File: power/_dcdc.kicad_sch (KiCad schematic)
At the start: 13 parts, among them U5 TPS56A37RPAR

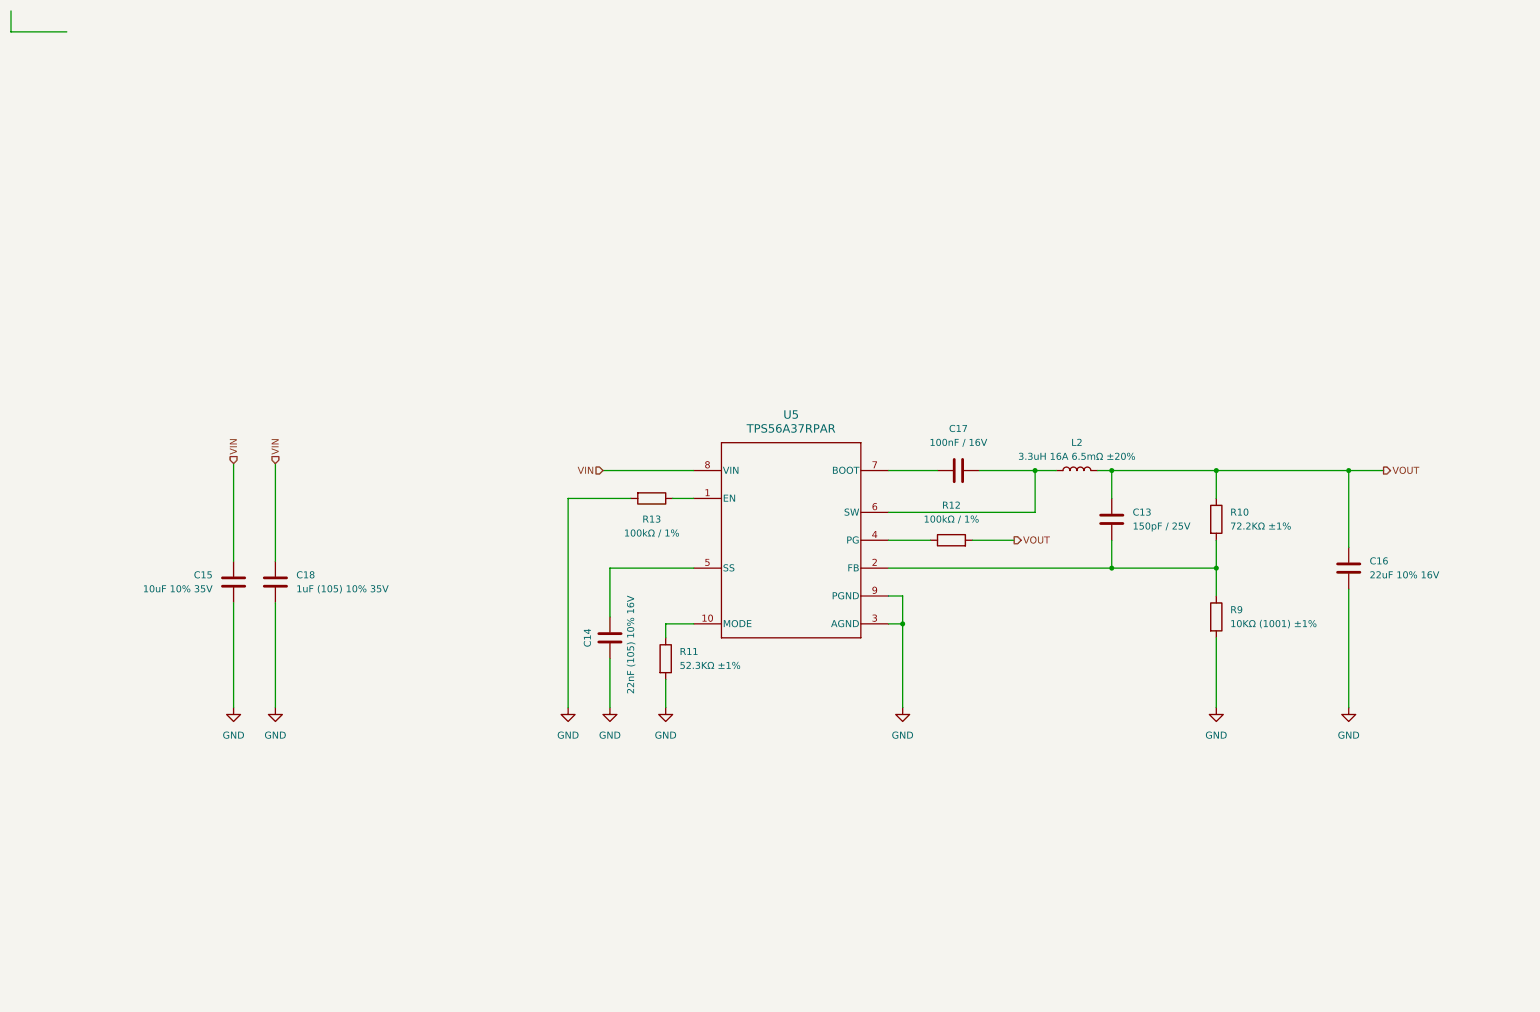
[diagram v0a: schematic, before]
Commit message: use TPS56A37 (preliminary commit with broken net tie via)
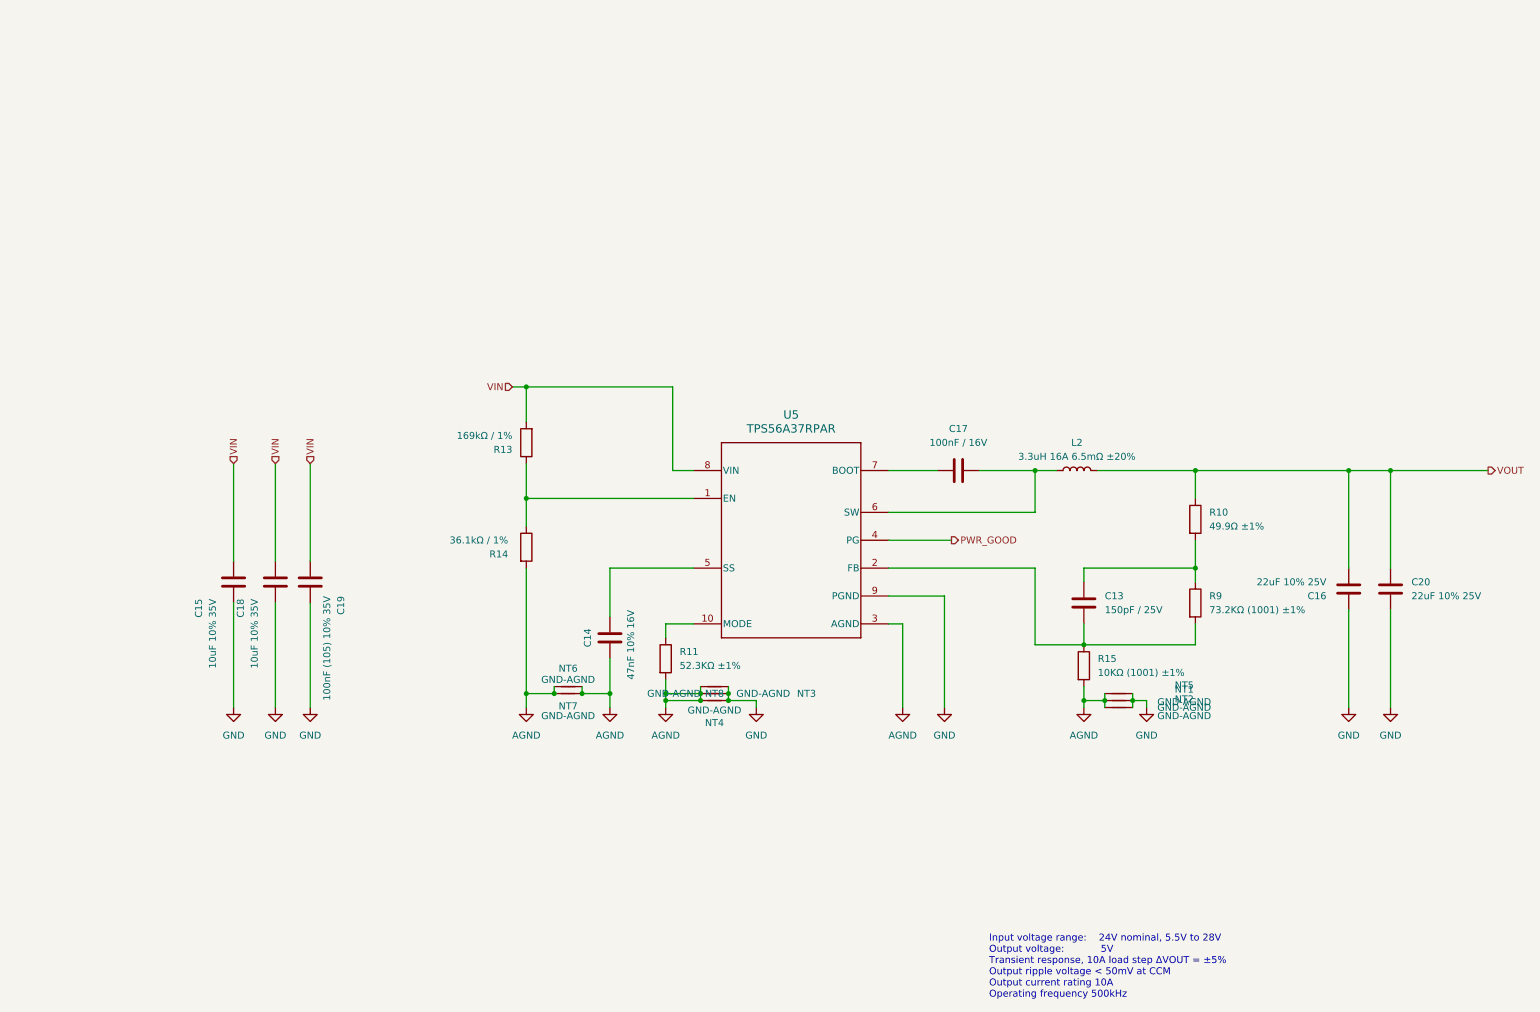
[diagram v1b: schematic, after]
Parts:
- removed R12: 100kΩ / 1%, Resistor_SMD:R_0603_1608Metric, symbol Device:R
- added C19: 100nF (105) 10% 35V, Capacitor_SMD:C_0603_1608Metric, symbol Device:C
- added C20: 22uF 10% 25V, Capacitor_SMD:C_1210_3225Metric, symbol Device:C
- added NT1, NT2, NT3, NT4, NT5, NT6, NT7, NT8: GND-AGND, pilotpi:NetTie-2_THT_Pad0.3mm, symbol Device:NetTie_2
- added R14: 36.1kΩ / 1%, Resistor_SMD:R_0603_1608Metric, symbol Device:R
- added R15: 10KΩ (1001) ±1%, Resistor_SMD:R_0402_1005Metric, symbol Device:R
- C13: Part C0603C151K3GACTU -> 0603B151K500NT
- C14: value 22nF (105) 10% 16V -> 47nF 10% 16V; footprint Capacitor_SMD:C_0402_1005Metric -> Resistor_SMD:R_0603_1608Metric; Part FN15X223K250PNG -> CL10B473KB8NNNC
- C15: Part HGC0805R5106K350NSLJ -> GRM21BR61H106KE43L
- C16: value 22uF 10% 16V -> 22uF 10% 25V; Part CL32B226KOJNNNE -> CL31A226KAHNNNE
- C17: footprint Capacitor_SMD:C_0603_1608Metric -> Resistor_SMD:R_0402_1005Metric; Part C0603B104J160NT -> CL05B104KO5NNNC
- C18: value 1uF (105) 10% 35V -> 10uF 10% 35V; footprint Capacitor_SMD:C_0603_1608Metric -> Capacitor_SMD:C_0805_2012Metric; Part C1608X7R1V105K080AC -> GRM21BR61H106KE43L
- R10: value 72.2KΩ ±1% -> 49.9Ω ±1%; footprint Resistor_SMD:R_0805_2012Metric -> Resistor_SMD:R_0402_1005Metric; Part RTT0573R2FTP -> RT0402BRE0749R9L
- R11: Part 0402WGF5232TCE -> ERA-2AEB5232X
- R13: value 100kΩ / 1% -> 169kΩ / 1%; Part RCA03100KFLF -> 0603WAF1693T5E
- R9: value 10KΩ (1001) ±1% -> 73.2KΩ (1001) ±1%; Part 1RC0402F1002 -> RT0402BRD0773K2L
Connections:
- net GND: now also C19.2, C20.2, NT1.1, NT2.1, NT3.1, NT4.1, NT5.1, NT8.2; no longer C14.2, R11.2, R13.2, R9.2, U5.3 (AGND)
- net VIN: now also R13.2, C19.1
- net VOUT: now also C20.1; no longer C13.1
- net at R10.2, R9.1: now also C13.1; no longer C13.2, U5.2 (FB)
- net at R13.1, U5.1 (EN): now also R14.1
- net PWR_GOOD: now reaches U5.4 (PG)
- new net: C13.2, R15.1, R9.2, U5.2 (FB)
- new net AGND: C14.2, NT1.2, NT2.2, NT3.2, NT4.2, NT5.2, NT6.1, NT6.2, NT7.1, NT7.2, NT8.1, R11.2, R14.2, R15.2, U5.3 (AGND)
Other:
- note added: "Input voltage range: 24V nominal, 5.5V to 28V Output voltage: 5V Transient response, 10A load step ΔVOUT = ±5% Output ripple voltage < 50mV at CCM Output current rating 10A Operating frequency 500kHz"
- moved on the sheet: C13, C16, R10, R13, R9

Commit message: preliminary complete layout
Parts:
- removed NT1, NT2, NT3, NT5, NT6, NT7, NT8: GND-AGND, pilotpi:NetTie-2_THT_Pad0.3mm, symbol Device:NetTie_2
- NT4: footprint pilotpi:NetTie-2_THT_Pad0.3mm -> NetTie:NetTie-2_THT_Pad0.3mm
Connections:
- net AGND: now also NT4.1; no longer NT4.2
- net GND: now also NT4.2; no longer NT4.1
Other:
- moved on the sheet: NT4, R13, R14

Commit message: use 75k for 5.1V output; use cheaper 0603 package
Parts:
- R9: value 73.2KΩ (1001) ±1% -> 75KΩ (1001) ±1%; footprint Resistor_SMD:R_0402_1005Metric -> Resistor_SMD:R_0603_1608Metric; Part RT0402BRD0773K2L -> 0603WAF7502T5E
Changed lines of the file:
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@@
 			)
 		)
-		(property "Value" "73.2KΩ (1001) ±1%"
+		(property "Value" "75KΩ (1001) ±1%"
 			(at 218.44 109.2199 0)
 			(show_name no)
@@
 			)
 		)
-		(property "Footprint" "Resistor_SMD:R_0402_1005Metric"
+		(property "Footprint" "Resistor_SMD:R_0603_1608Metric"
 			(at 214.122 107.95 90)
 			(hide yes)
@@
 			)
 		)
-		(property "Part" "RT0402BRD0773K2L"
+		(property "Part" "0603WAF7502T5E"
 			(at 215.9 107.95 0)
 			(hide yes)
+			(show_name no)
+			(do_not_autoplace no)
+			(effects
+				(font
+					(size 1.27 1.27)
+				)
+			)
+		)
+		(property "Field6" ""
+			(at 215.9 107.95 0)
+			(hide yes)

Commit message: change package of C16 and C20; add ChatGPT generated logo; use 220nF instead 330nF for C11
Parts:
- C16, C20: footprint Capacitor_SMD:C_1210_3225Metric -> Capacitor_SMD:C_1206_3216Metric
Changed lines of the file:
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@@
 		(in_bom no)
 		(on_board yes)
-		(in_pos_files yes)
+		(in_pos_files no)
 		(dnp no)
 		(property "Reference" "NT4"
@@
 			)
 		)
-		(property "Footprint" "Capacitor_SMD:C_1210_3225Metric"
+		(property "Footprint" "Capacitor_SMD:C_1206_3216Metric"
 			(at 244.8052 109.22 0)
 			(hide yes)
@@
 			)
 		)
-		(property "Footprint" "Capacitor_SMD:C_1210_3225Metric"
+		(property "Footprint" "Capacitor_SMD:C_1206_3216Metric"
 			(at 252.4252 109.22 0)
 			(hide yes)

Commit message: replace inductor
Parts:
- L2: footprint Inductor_SMD:L_Chilisin_BMRB00060612 -> Inductor_SMD:L_Sunlord_SWPA6045S; Part MHCC12050-3R3M-R7 -> MHCI06040-3R3M-R8
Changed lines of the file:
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@@
 			)
 		)
-		(property "Footprint" "Inductor_SMD:L_Chilisin_BMRB00060612"
+		(property "Footprint" "Inductor_SMD:L_Sunlord_SWPA6045S"
 			(at 194.31 83.82 0)
 			(hide yes)
@@
 			)
 		)
-		(property "Part" "MHCC12050-3R3M-R7"
+		(property "Part" "MHCI06040-3R3M-R8"
 			(at 194.31 83.82 0)
 			(hide yes)

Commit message: add custom inductor footprint
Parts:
- L2: footprint Inductor_SMD:L_Sunlord_SWPA6045S -> pilotpi:L_6.6x7.5_H4
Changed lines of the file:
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@@
 			)
 		)
-		(property "Footprint" "Inductor_SMD:L_Sunlord_SWPA6045S"
+		(property "Footprint" "pilotpi:L_6.6x7.5_H4"
 			(at 194.31 83.82 0)
 			(hide yes)
